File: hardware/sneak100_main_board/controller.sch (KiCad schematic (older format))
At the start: 17 parts, among them J10 Conn_01x02, U9 STM32F405RGTx, Y1 8MHz

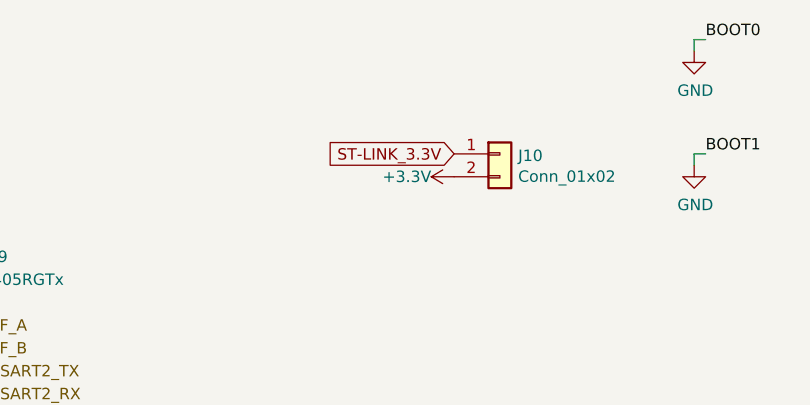
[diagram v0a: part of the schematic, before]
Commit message: More space in top hull and schematic fix
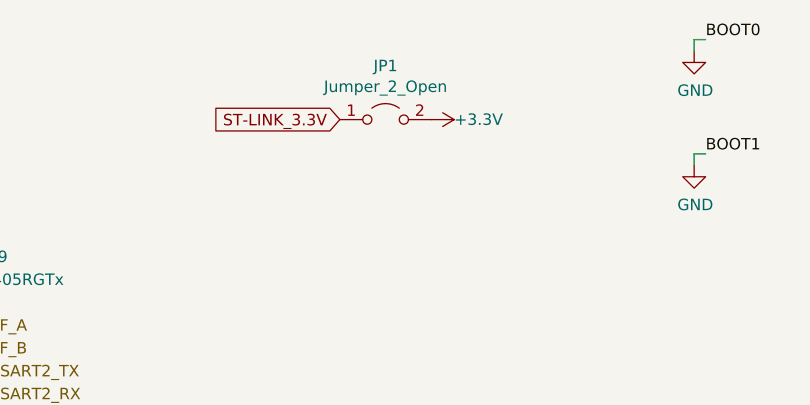
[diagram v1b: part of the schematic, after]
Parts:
- removed J10: Conn_01x02, Connector_PinHeader_2.54mm:PinHeader_1x02_P2.54mm_Vertical, symbol Connector_Generic:Conn_01x02
- added JP1: Jumper_2_Open, Connector_PinHeader_2.54mm:PinHeader_2x01_P2.54mm_Vertical, symbol Jumper:Jumper_2_Open
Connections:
- net +3V3: now also JP1.2 (B)
- net ST-LINK_3.3V: now also JP1.1 (A)
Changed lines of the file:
@@
 BOOT1
 $Comp
-L power:GND #PWR085
+L power:GND #PWR086
 U 1 1 60F14427
 P 7800 1600
-F 0 "#PWR085" H 7800 1350 50  0001 C CNN
+F 0 "#PWR086" H 7800 1350 50  0001 C CNN
 F 1 "GND" H 7805 1427 50  0000 C CNN
 F 2 "" H 7800 1600 50  0001 C CNN
@@
 NoConn ~ 3250 5400
 $Comp
-L power:+3.3V #PWR086
+L power:+3.3V #PWR085
 U 1 1 60FC5347
-P 6750 1650
-F 0 "#PWR086" H 6750 1500 50  0001 C CNN
-F 1 "+3.3V" V 6750 1750 50  0000 L CNN
-F 2 "" H 6750 1650 50  0001 C CNN
-F 3 "" H 6750 1650 50  0001 C CNN
-	1    6750 1650
-	0    -1   -1   0
+P 6650 1400
+F 0 "#PWR085" H 6650 1250 50  0001 C CNN
+F 1 "+3.3V" V 6650 1500 50  0000 L CNN
+F 2 "" H 6650 1400 50  0001 C CNN
+F 3 "" H 6650 1400 50  0001 C CNN
+	1    6650 1400
+	0    1    1    0
 $EndComp
 Text GLabel 6900 3300 2    50   Input ~ 0
@@
 Text GLabel 6900 3400 2    50   Input ~ 0
 ST-LINK_3.3V
-Text GLabel 6750 1550 0    50   Input ~ 0
-ST-LINK_3.3V
-$Comp
-L Connector_Generic:Conn_01x02 J10
-U 1 1 6106012F
-P 6950 1550
-F 0 "J10" H 7030 1542 50  0000 L CNN
-F 1 "Conn_01x02" H 7030 1451 50  0000 L CNN
-F 2 "Connector_PinHeader_2.54mm:PinHeader_1x02_P2.54mm_Vertical" H 6950 1550 50  0001 C CNN
-F 3 "~" H 6950 1550 50  0001 C CNN
-	1    6950 1550
-	1    0    0    -1
-$EndComp
 Text Label 7850 1050 0    50   ~ 0
 BOOT0
@@
 NoConn ~ 4650 3400
 NoConn ~ 4650 3500
+$Comp
+L Jumper:Jumper_2_Open JP1
+U 1 1 60FDB1A1
+P 6450 1400
+F 0 "JP1" H 6450 1635 50  0000 C CNN
+F 1 "Jumper_2_Open" H 6450 1544 50  0000 C CNN
+F 2 "Connector_PinHeader_2.54mm:PinHeader_2x01_P2.54mm_Vertical" H 6450 1400 50  0001 C CNN
+F 3 "~" H 6450 1400 50  0001 C CNN
+	1    6450 1400
+	1    0    0    -1
+$EndComp
+Text GLabel 6250 1400 0    50   Input ~ 0
+ST-LINK_3.3V
 $EndSCHEMATC

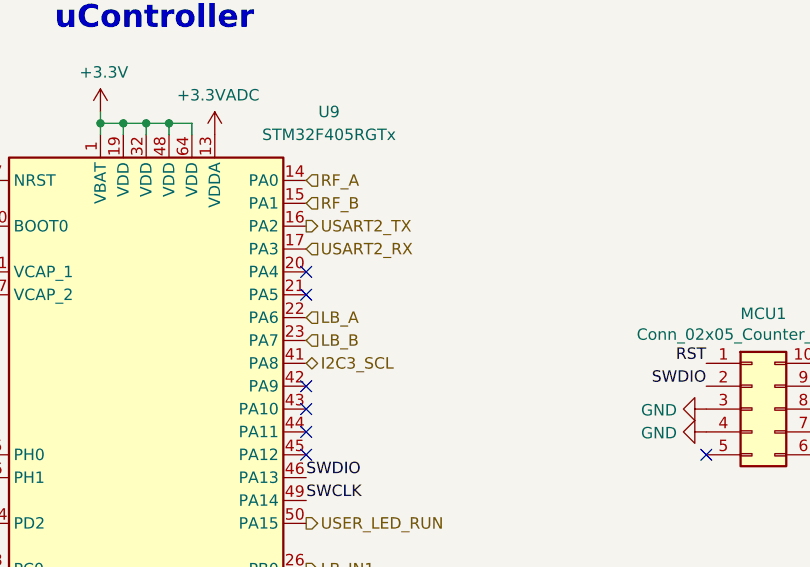
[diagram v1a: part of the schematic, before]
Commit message: bluetooth en & status connection
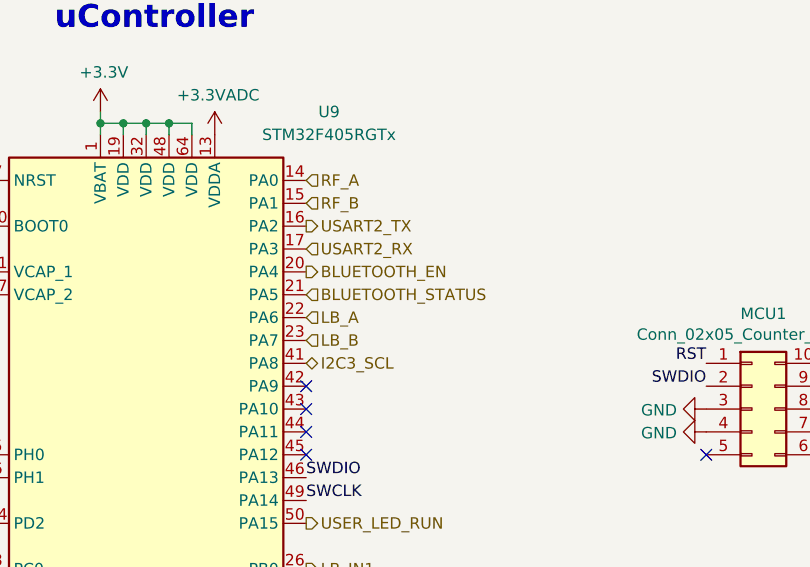
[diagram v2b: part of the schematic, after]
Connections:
- net BLUETOOTH_EN: now reaches U9.20 (PA4)
- net BLUETOOTH_STATUS: now reaches U9.21 (PA5)
- no-connect marks 13 -> 11
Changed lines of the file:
@@
 Text HLabel 4650 2600 2    50   Input ~ 0
 USART2_RX
-NoConn ~ 4650 2700
-NoConn ~ 4650 2800
 Text HLabel 4650 2900 2    50   Input ~ 0
 LB_A
@@
 Text GLabel 6250 1400 0    50   Input ~ 0
 ST-LINK_3.3V
+Text HLabel 4650 2700 2    50   Output ~ 0
+BLUETOOTH_EN
+Text HLabel 4650 2800 2    50   Input ~ 0
+BLUETOOTH_STATUS
 $EndSCHEMATC

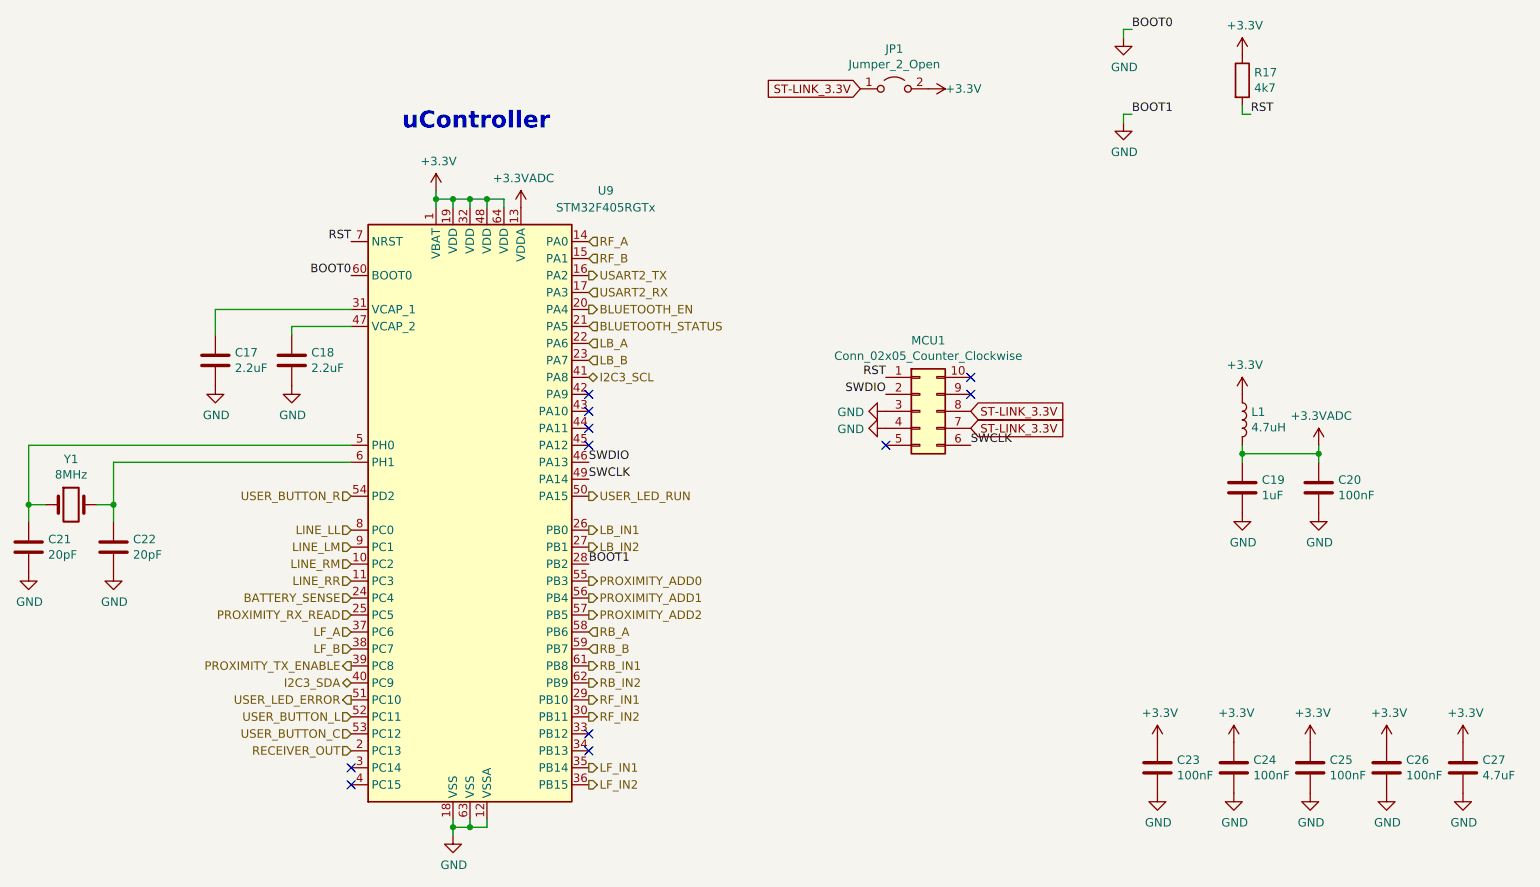
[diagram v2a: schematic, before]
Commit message: Add external proximity sensor, erase old from schematic
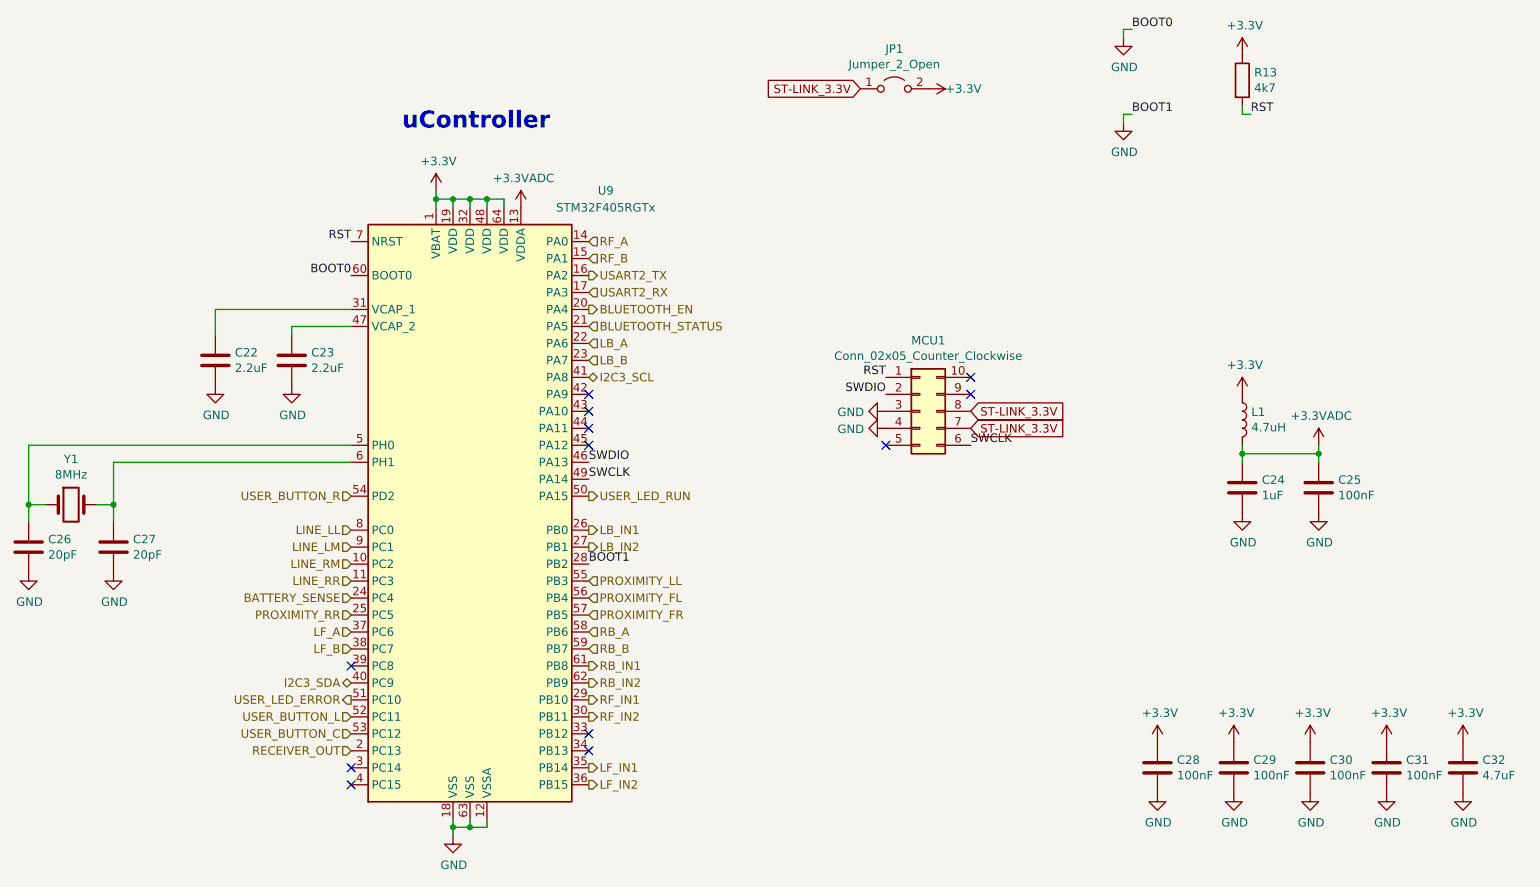
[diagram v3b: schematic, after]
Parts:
- renumbered C17 to C22, C18 to C23, C19 to C24, C20 to C25, C21 to C26, C22 to C27, C23 to C28, C24 to C29, C25 to C30, C26 to C31, C27 to C32, R17 to R13
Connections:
- net PROXIMITY_ADD0 renamed PROXIMITY_LL
- net PROXIMITY_ADD1 renamed PROXIMITY_FL
- net PROXIMITY_ADD2 renamed PROXIMITY_FR
- net PROXIMITY_RX_READ renamed PROXIMITY_RR
- net PROXIMITY_TX_ENABLE: no longer names the net of U9.39 (PC8)
- no-connect marks 11 -> 12

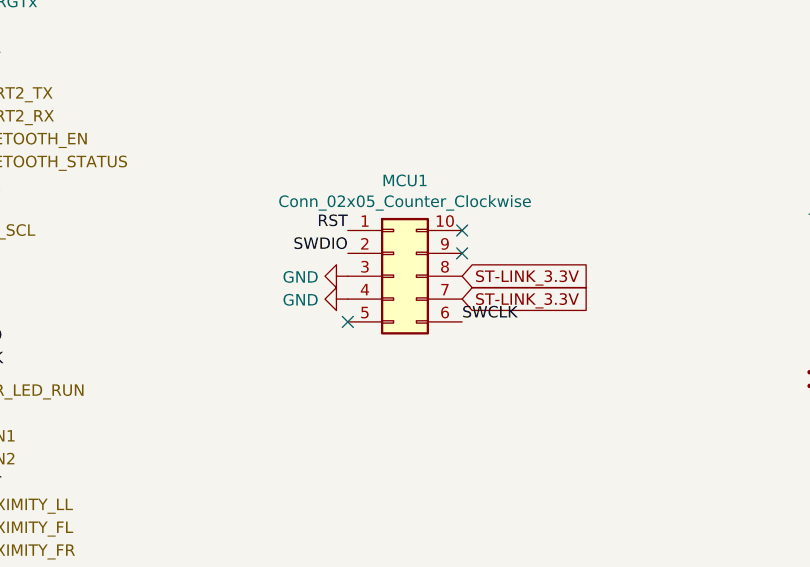
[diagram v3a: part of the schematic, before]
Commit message: line sensors connectors
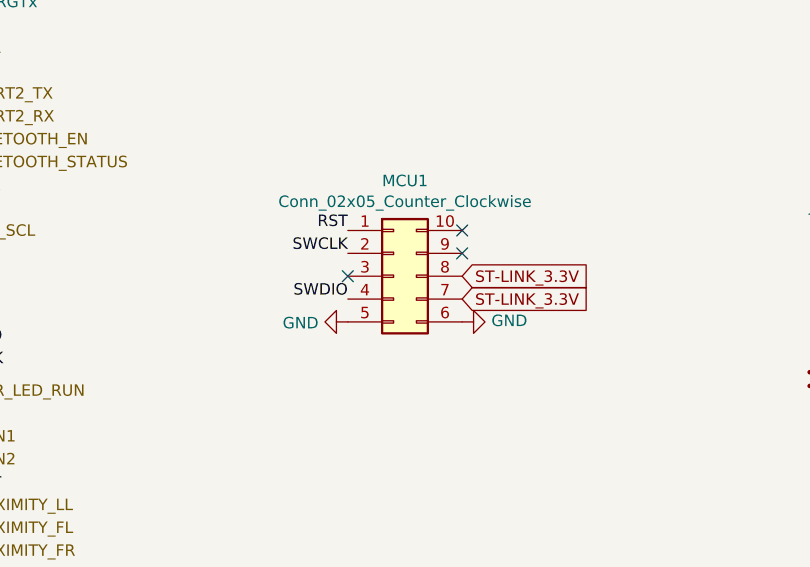
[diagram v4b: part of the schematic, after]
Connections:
- net GND: now also MCU1.5 (Pin_5), MCU1.6 (Pin_6); no longer MCU1.3 (Pin_3), MCU1.4 (Pin_4)
- net SWCLK: now also MCU1.2 (Pin_2); no longer MCU1.6 (Pin_6)
- net SWDIO: now also MCU1.4 (Pin_4); no longer MCU1.2 (Pin_2)
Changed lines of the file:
@@
 NoConn ~ 6900 3200
 NoConn ~ 6900 3100
-NoConn ~ 6400 3500
+NoConn ~ 6400 3300
 $Comp
 L power:GND #PWR097
 U 1 1 60244908
-P 6400 3400
-F 0 "#PWR097" H 6400 3150 50  0001 C CNN
-F 1 "GND" V 6405 3272 50  0000 R CNN
-F 2 "" H 6400 3400 50  0001 C CNN
-F 3 "" H 6400 3400 50  0001 C CNN
-	1    6400 3400
-	0    1    1    0
+P 6900 3500
+F 0 "#PWR097" H 6900 3250 50  0001 C CNN
+F 1 "GND" V 6905 3372 50  0000 R CNN
+F 2 "" H 6900 3500 50  0001 C CNN
+F 3 "" H 6900 3500 50  0001 C CNN
+	1    6900 3500
+	0    -1   -1   0
 $EndComp
 $Comp
 L power:GND #PWR096
 U 1 1 60244902
-P 6400 3300
-F 0 "#PWR096" H 6400 3050 50  0001 C CNN
-F 1 "GND" V 6405 3172 50  0000 R CNN
-F 2 "" H 6400 3300 50  0001 C CNN
-F 3 "" H 6400 3300 50  0001 C CNN
-	1    6400 3300
+P 6400 3500
+F 0 "#PWR096" H 6400 3250 50  0001 C CNN
+F 1 "GND" V 6405 3372 50  0000 R CNN
+F 2 "" H 6400 3500 50  0001 C CNN
+F 3 "" H 6400 3500 50  0001 C CNN
+	1    6400 3500
 	0    1    1    0
 $EndComp
@@
 Text Label 4650 3700 0    50   ~ 0
 SWCLK
+Text Label 6400 3400 2    50   ~ 0
+SWDIO
 Text Label 6400 3200 2    50   ~ 0
-SWDIO
-Text Label 6900 3500 0    50   ~ 0
 SWCLK
 Text Notes 3550 1650 0    100  ~ 20

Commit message: Motor signals and interface
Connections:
- net RB_A: now also U9.14 (PA0); no longer U9.58 (PB6)
- net RB_B: now also U9.15 (PA1); no longer U9.59 (PB7)
- net RB_IN1: now also U9.29 (PB10); no longer U9.61 (PB8)
- net RB_IN2: now also U9.30 (PB11); no longer U9.62 (PB9)
- net RF_A: now also U9.58 (PB6); no longer U9.14 (PA0)
- net RF_B: now also U9.59 (PB7); no longer U9.15 (PA1)
- net RF_IN1: now also U9.61 (PB8); no longer U9.29 (PB10)
- net RF_IN2: now also U9.62 (PB9); no longer U9.30 (PB11)
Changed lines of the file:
@@
 Text Notes 3550 1650 0    100  ~ 20
 uController
-Text HLabel 4650 2300 2    50   Input ~ 0
+Text HLabel 4650 4600 2    50   Input ~ 0
 RF_A
-Text HLabel 4650 2400 2    50   Input ~ 0
+Text HLabel 4650 4700 2    50   Input ~ 0
 RF_B
 Text HLabel 4650 2500 2    50   Output ~ 0
@@
 Text HLabel 4650 4500 2    50   Input ~ 0
 PROXIMITY_FR
-Text HLabel 4650 4600 2    50   Input ~ 0
+Text HLabel 4650 2300 2    50   Input ~ 0
 RB_A
-Text HLabel 4650 4700 2    50   Input ~ 0
+Text HLabel 4650 2400 2    50   Input ~ 0
 RB_B
+Text HLabel 4650 5000 2    50   Output ~ 0
+RB_IN1
+Text HLabel 4650 5100 2    50   Output ~ 0
+RB_IN2
 Text HLabel 4650 4800 2    50   Output ~ 0
-RB_IN1
+RF_IN1
 Text HLabel 4650 4900 2    50   Output ~ 0
-RB_IN2
-Text HLabel 4650 5000 2    50   Output ~ 0
-RF_IN1
-Text HLabel 4650 5100 2    50   Output ~ 0
 RF_IN2
 NoConn ~ 4650 5200

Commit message: Remaining signals from uC
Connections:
- net LINE_LL: now also U9.11 (PC3); no longer U9.8 (PC0)
- net LINE_LM: now also U9.10 (PC2); no longer U9.9 (PC1)
- net LINE_RM: now also U9.9 (PC1); no longer U9.10 (PC2)
- net LINE_RR: now also U9.8 (PC0); no longer U9.11 (PC3)
- net PROXIMITY_FL: now also U9.25 (PC5); no longer U9.56 (PB4)
- net PROXIMITY_RR: now also U9.56 (PB4); no longer U9.25 (PC5)
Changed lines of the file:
@@
 Text HLabel 4650 4300 2    50   Input ~ 0
 PROXIMITY_LL
-Text HLabel 4650 4400 2    50   Input ~ 0
+Text HLabel 3250 4500 0    50   Input ~ 0
 PROXIMITY_FL
-Text HLabel 4650 4500 2    50   Input ~ 0
-PROXIMITY_FR
 Text HLabel 4650 2300 2    50   Input ~ 0
 RB_A
@@
 Text HLabel 3250 5300 0    50   Input ~ 0
 RECEIVER_OUT
+Text HLabel 3250 4300 0    50   Input ~ 0
+LINE_LL
+Text HLabel 3250 4200 0    50   Input ~ 0
+LINE_LM
+Text HLabel 3250 4100 0    50   Input ~ 0
+LINE_RM
 Text HLabel 3250 4000 0    50   Input ~ 0
-LINE_LL
-Text HLabel 3250 4100 0    50   Input ~ 0
-LINE_LM
-Text HLabel 3250 4200 0    50   Input ~ 0
-LINE_RM
-Text HLabel 3250 4300 0    50   Input ~ 0
 LINE_RR
 Text HLabel 3250 4400 0    50   Input ~ 0
 BATTERY_SENSE
-Text HLabel 3250 4500 0    50   Input ~ 0
-PROXIMITY_RR
 Text HLabel 3250 4600 0    50   Input ~ 0
 LF_A
@@
 BLUETOOTH_STATUS
 NoConn ~ 3250 4800
+Text HLabel 4650 4500 2    50   Input ~ 0
+PROXIMITY_FR
+Text HLabel 4650 4400 2    50   Input ~ 0
+PROXIMITY_RR
 $EndSCHEMATC

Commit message: programmer connector, proximity sensors routed
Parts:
- removed MCU1: Conn_02x05_Counter_Clockwise, Connector_IDC:IDC-Header_2x05_P2.54mm_Vertical, symbol Connector_Generic:Conn_02x05_Counter_Clockwise
- added J13: Conn_02x05_Odd_Even, Connector_IDC:IDC-Header_2x05_P2.54mm_Vertical, symbol Connector_Generic:Conn_02x05_Odd_Even
- renumbered C26 to C24, C27 to C25, C24 to C26, C25 to C27
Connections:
- net +3V3: no longer JP1.2 (B)
- net GND: now also J13.5 (Pin_5), J13.6 (Pin_6)
- net RST: now also J13.1 (Pin_1)
- net SWCLK: now also J13.2 (Pin_2)
- net SWDIO: now also J13.4 (Pin_4)
- net ST-LINK_3.3V renamed ST-LINK_5V
- net ST-LINK_5V: now also J13.10 (Pin_10), J13.9 (Pin_9)
- new net +5V: JP1.2 (B)
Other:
- note added: "ST-LINK V2"
- note added: "uC programmer"
- moved on the sheet: C26, C27, JP1, L1, R13

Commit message: component list and values fix
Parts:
- C24, C25: value 20pF -> 22pF
- R13: value 4k7 -> 10k
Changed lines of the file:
@@
 AR Path="/6100FE40/60060D9D" Ref="R13"  Part="1"
 F 0 "R13" H 9420 1696 50  0000 L CNN
-F 1 "4k7" H 9420 1605 50  0000 L CNN
+F 1 "10k" H 9420 1605 50  0000 L CNN
 F 2 "Resistor_SMD:R_0603_1608Metric" V 9280 1650 50  0001 C CNN
 F 3 "~" H 9350 1650 50  0001 C CNN
@@
 AR Path="/6100FE40/60060E51" Ref="C24"  Part="1"
 F 0 "C24" H 1465 4146 50  0000 L CNN
-F 1 "20pF" H 1465 4055 50  0000 L CNN
+F 1 "22pF" H 1465 4055 50  0000 L CNN
 F 2 "Capacitor_SMD:C_0603_1608Metric" H 1388 3950 50  0001 C CNN
 F 3 "~" H 1350 4100 50  0001 C CNN
@@
 AR Path="/6100FE40/60060E57" Ref="C25"  Part="1"
 F 0 "C25" H 1965 4146 50  0000 L CNN
-F 1 "20pF" H 1965 4055 50  0000 L CNN
+F 1 "22pF" H 1965 4055 50  0000 L CNN
 F 2 "Capacitor_SMD:C_0603_1608Metric" H 1888 3950 50  0001 C CNN
 F 3 "~" H 1850 4100 50  0001 C CNN
